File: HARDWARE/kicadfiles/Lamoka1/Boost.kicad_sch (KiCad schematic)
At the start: 35 parts, among them Q4 NMOS

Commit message: Improve on the values for the schematic of boost converter
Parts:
- C1: value C1206C474K5RACTU -> 0.47u
- C2: value CC0603KRX7R9BB223 -> 22n
- C25, C26: value UUX2A470MNL1GS -> 47u
- C27, C32: value UCD2A220MNL1GS -> 22u
- C28: value CL10B104KB8NNNC -> 100n
- C30: value KRM55WR72A226MH01L -> 22u
- C31: value UCD2A101MNJ1MS -> 10u
- Cbst7: value C1206C224M1REC7210 -> 220n
- Cbst8: value C1206C224M1REC7210 -> 0.22u
- Cvcc7: value CNC5L1X7R1H106K160AE -> 100n
- Cvcc8: value CNC5L1X7R1H106K160AE -> 10u
- R1: value RC0603FR-0756K2L -> 56.2k
- R2: value RN73R1JTTD1842F25 -> 18.4k
- R3: value RC0603FR-07392KL -> 392k
- R35, R37, R38: value RC0603FR-0736KL -> 36k
- R39, R40: value TLRP3A30CR005FTE -> 5m
- R4: value RC0603FR-0710KL -> 10k
- R5: value RN73R1JTTD4992F25 -> 49.9k
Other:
- moved on the sheet: C30, C31, C32, Q4, R38, R41

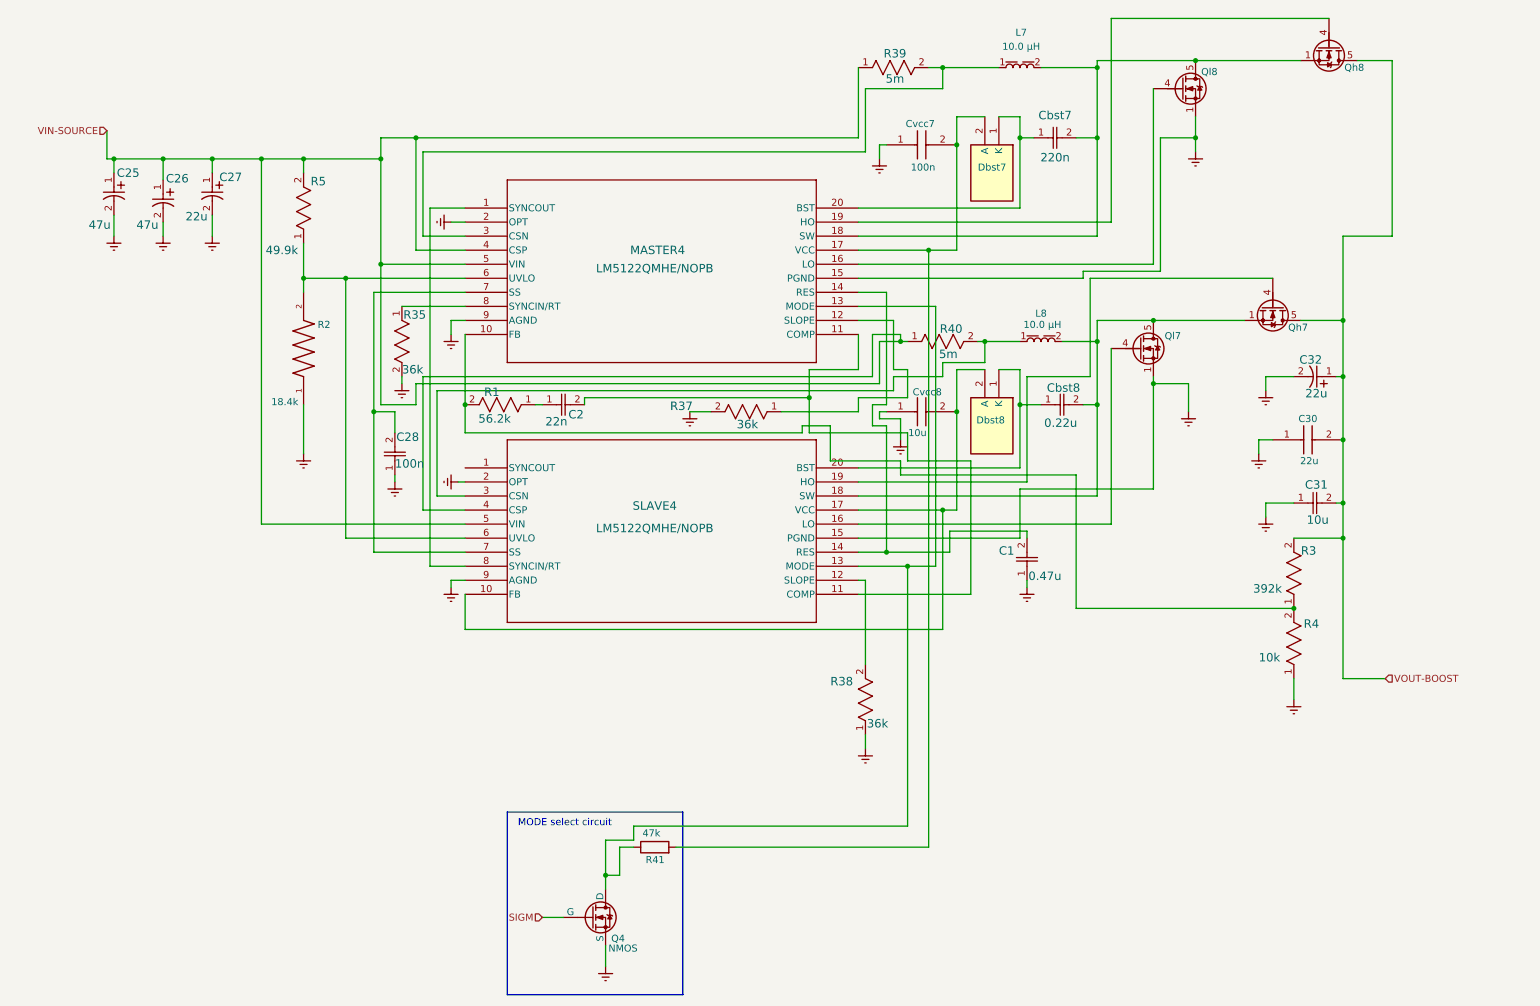
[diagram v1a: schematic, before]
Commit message: FIX values and add info
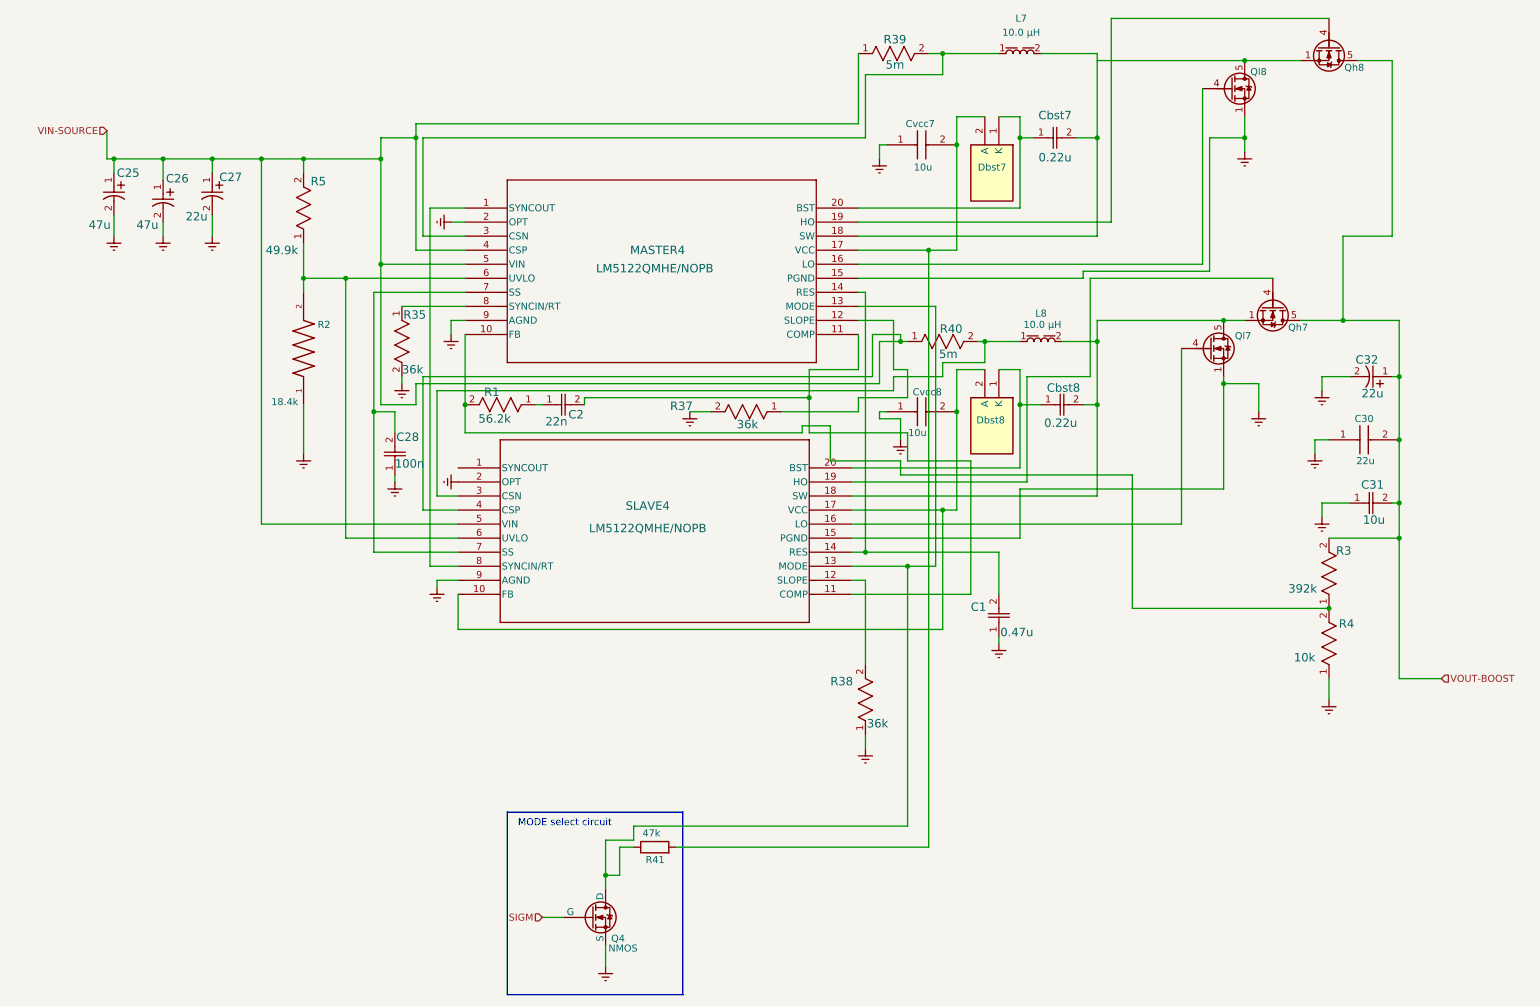
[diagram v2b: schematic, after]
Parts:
- Cbst7: value 220n -> 0.22u
- Cvcc7: value 100n -> 10u
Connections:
- net at Qh8.1 (S), Qh8.2 (S), Qh8.3 (S)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: no longer Cbst7.2, L7.2, MASTER4.18 (SW)
- new net: Cbst7.2, L7.2, MASTER4.18 (SW)
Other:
- company: (none) -> Flamingo-n-Cactus
- title: (none) -> Boost-section
- moved on the sheet: C1, C30, C31, C32, L7, Ql7, Ql8, R3, R39, R4, SLAVE4

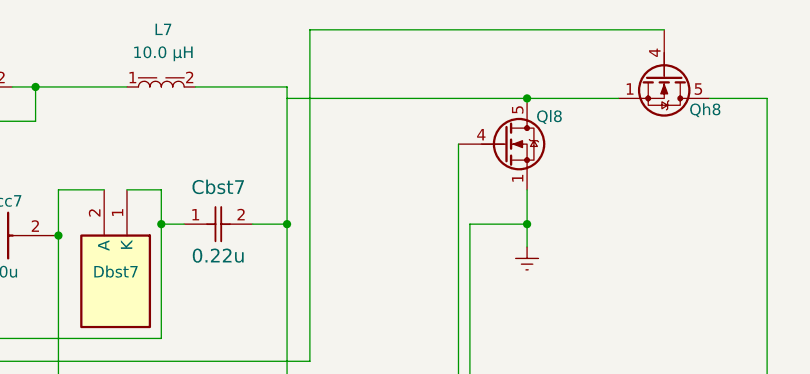
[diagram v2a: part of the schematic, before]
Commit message: URGENT had to fix a connection
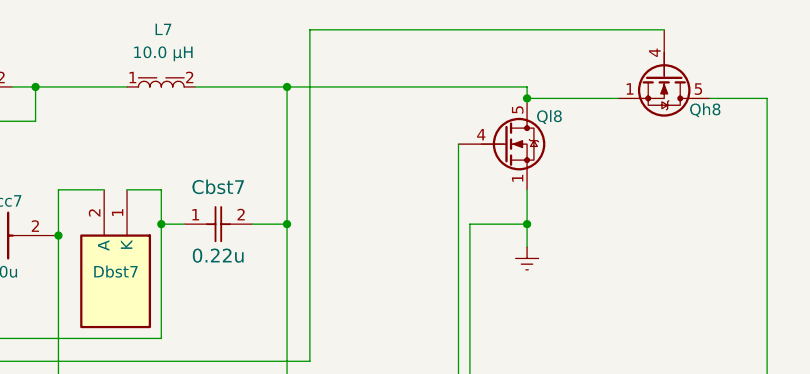
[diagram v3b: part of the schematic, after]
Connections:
- net at Qh8.1 (S), Qh8.2 (S), Qh8.3 (S)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: now also Cbst7.2, L7.2, MASTER4.18 (SW)
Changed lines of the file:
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@@
+	)
+	(junction
+		(at 205.74 22.86)
+		(diameter 0)
+		(color 0 0 0 0)
 	)
 	(junction
@@
 	(wire
 		(pts
-			(xy 205.74 24.13) (xy 232.41 24.13)
+			(xy 205.74 22.86) (xy 232.41 22.86)
 		)
 		(stroke
@@
 		)
 		(stroke
+			(width 0)
+			(type default)
+		)
+	)
+	(wire
+		(pts
+			(xy 232.41 22.86) (xy 232.41 24.13)
+		)
+		(stroke

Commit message: REAL actually fixing it for the net system
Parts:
- removed C28: 100n, Components:CAP_CL10_SAM, symbol 2026-06-24_20-27-18:CL10B104KB8NNNC
- removed C30: 22u, Components:CAPC6153X670N, symbol KRM55WR72A226MH01L:KRM55WR72A226MH01L
- removed C31: 10u, Components:CAP_UCD2A_NCH, symbol 2026-06-23_14-35-42:UCD2A101MNJ1MS
- removed C32: 22u, Components:PCAP_8x10-ELECT_NCH, symbol 2026-06-22_18-02-40:UCD2A220MNL1GS
- removed Q4: NMOS, symbol Simulation_SPICE:NMOS
- removed R35, R37: 36k, Components:RC0603N_YAG, symbol 2026-06-24_19-49-47:RC0603FR-0736KL
- added C29: 100n, Components:CAP_CL10_SAM, symbol 2026-06-24_20-27-18:CL10B104KB8NNNC
- added C33: 22u, Components:CAPC6153X670N, symbol KRM55WR72A226MH01L:KRM55WR72A226MH01L
- added C34: 10u, Components:CAP_UCD2A_NCH, symbol 2026-06-23_14-35-42:UCD2A101MNJ1MS
- added C35: 22u, Components:PCAP_8x10-ELECT_NCH, symbol 2026-06-22_18-02-40:UCD2A220MNL1GS
- added R36, R42: 36k, Components:RC0603N_YAG, symbol 2026-06-24_19-49-47:RC0603FR-0736KL
- added U1: AO3400A, Components:SOT-23-3L_AOS, symbol 2026-06-29_16-51-38:AO3400A
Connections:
- net Earth: now also C29.1, C33.1, C34.1, C35.2, R36.2, R42.2, U1.2 (S)
- net SIGM: now also U1.1 (G)
- net VOUT-BOOST: now also C33.2, C34.2, C35.1
- net BSTS: now reaches Cbst8.1, Dbst8.1 (K), SLAVE4.20 (BST)
- net SWS: now reaches Cbst8.2, L8.2, Qh7.1 (S), Qh7.2 (S), Qh7.3 (S), Ql7.5 (D), SLAVE4.18 (SW)
- net MODE: now reaches MASTER4.13 (MODE), R41.1, SLAVE4.13 (MODE)
- net MODE: now also U1.3 (D)
- net VCCM: now reaches Cvcc7.2, Dbst7.2 (A), MASTER4.17 (VCC), R41.2
- net BSTM: now reaches Cbst7.1, Dbst7.1 (K), MASTER4.20 (BST)
- net UVLO: now reaches MASTER4.6 (UVLO), R2.2, R5.1, SLAVE4.6 (UVLO)
- net SYNCIN/RTM: now reaches MASTER4.8 (SYNCIN/RT)
- net SYNCIN/RTM: now also R36.1
- net LOS: now reaches Ql7.4 (G), SLAVE4.16 (LO)
- net SS: now reaches MASTER4.7 (SS), SLAVE4.7 (SS)
- net SS: now also C29.2
- net FBS: now reaches Cvcc8.2, Dbst8.2 (A), SLAVE4.10 (FB), SLAVE4.17 (VCC)
- net FBM: now reaches MASTER4.10 (FB), R1.2, R3.1, R4.2
- net LOM: now reaches MASTER4.16 (LO), Ql8.4 (G)
- net SWM: now reaches Cbst7.2, L7.2, MASTER4.18 (SW), Qh8.1 (S), Qh8.2 (S), Qh8.3 (S), Ql8.5 (D)
- net HOM: now reaches MASTER4.19 (HO), Qh8.4 (G)
- net CSNS: now reaches L8.1, R40.2, SLAVE4.3 (CSN)
- net RES: now reaches C1.2, MASTER4.14 (RES), SLAVE4.14 (RES)
- net CSNM: now reaches L7.1, MASTER4.3 (CSN), R39.2
- net SYNCIN/RTS: now reaches MASTER4.1 (SYNCOUT), SLAVE4.8 (SYNCIN/RT)
- net COMP: now reaches C2.2, MASTER4.11 (COMP), SLAVE4.11 (COMP)
- net SLOPEM: now reaches MASTER4.12 (SLOPE)
- net SLOPEM: now also R42.1
- net HOS: now reaches Qh7.4 (G), SLAVE4.19 (HO)
- net SLOPES: now reaches R38.2, SLAVE4.12 (SLOPE)
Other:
- moved on the sheet: C1, C2, C25, C26, C27, Cbst7, Cbst8, Cvcc7, Cvcc8, Dbst7, Dbst8, L7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

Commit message: ADD more misc "housekeeping" work for boost converter
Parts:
- removed C34: 10u, Components:CAP_UCD2A_NCH, symbol 2026-06-23_14-35-42:UCD2A101MNJ1MS
- added C36: 10u, Components:CAP_UCD2A_NCH, symbol 2026-06-23_14-35-42:UCD2A101MNJ1MS
- added TP1, TP3, TP4, TP5: Tomachie_TP_N, TestPoint:TestPoint_Pad_D2.0mm, symbol Pads:Tomachie_TP_N
- added TP2: Tomachie_TP_S, TestPoint:TestPoint_Pad_D2.0mm, symbol Pads:Tomachie_TP_S
- added TP6, TP7, TP8: Tomachie_TP_W, TestPoint:TestPoint_Pad_D2.0mm, symbol Pads:Tomachie_TP_W
- L7, L8: Critical Parameter 10.0 µH -> 10u
- renumbered Cvcc7 to C3, Cbst7 to C4, Cvcc8 to C5, Cbst8 to C6, Dbst7 to D7, Dbst8 to D8, Ql8 to Q1, Qh8 to Q2, Ql7 to Q3, Qh7 to Q4, U1 to Q5, MASTER4 to U2, SLAVE4 to U3
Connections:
- net CSNM: now also TP1.1
- net CSNS: now also TP2.1
- net Earth: now also C36.2, TP3.1, TP4.1, TP5.1, TP6.1, TP7.1, TP8.1
- net VOUT-BOOST: now also C36.1
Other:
- note added: "SIGM = Connection to signal (MODE select)"
- note added: "VIN-SOURCE = 5-40V"
- note added: "VOUT-BOOST = 48v"
- moved on the sheet: C1, C2, C3, C33, C35, C4, C5, C6, D7, D8, L7, L8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

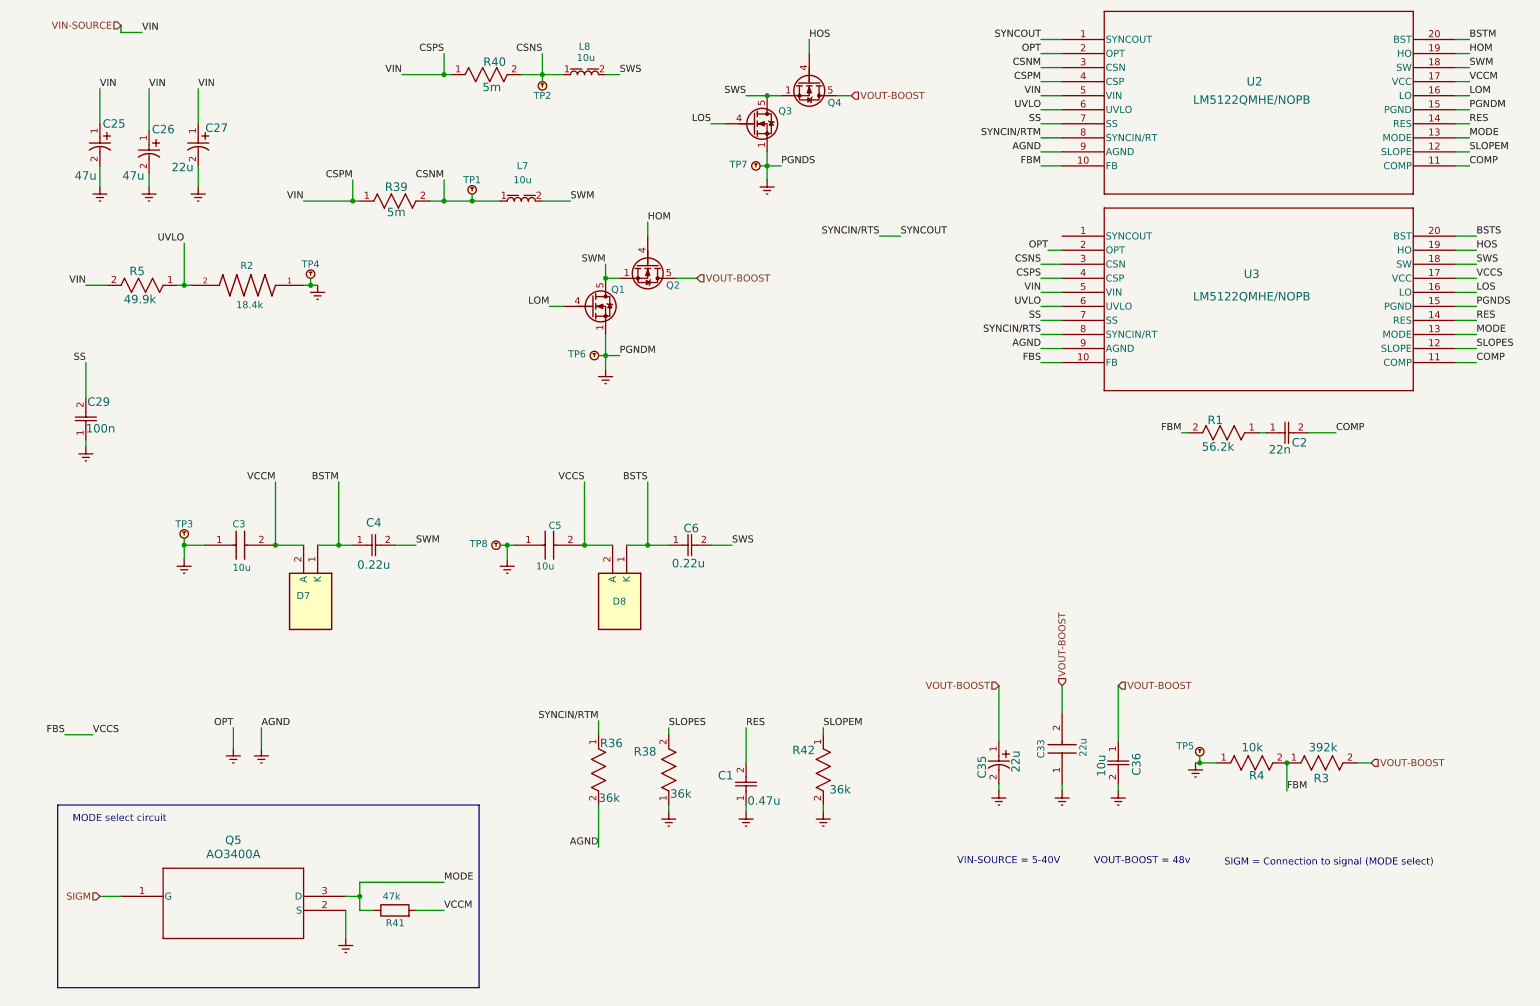
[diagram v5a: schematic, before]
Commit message: Make boost schem more neat, ADD top priority image
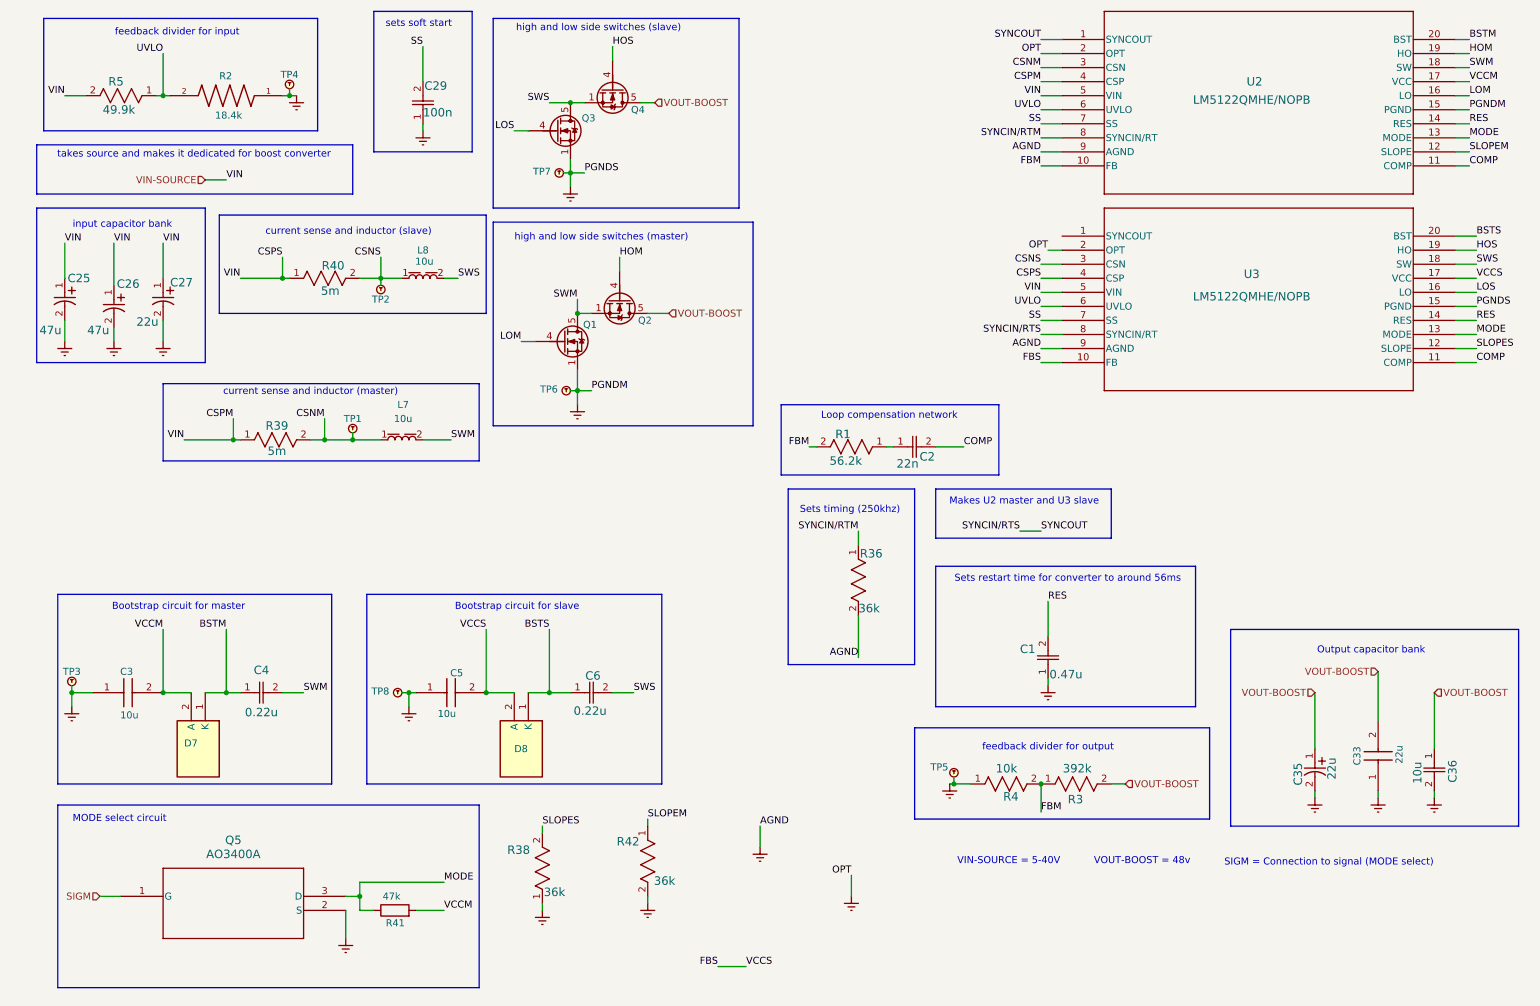
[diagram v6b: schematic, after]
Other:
- note added: "Bootstrap circuit for master"
- note added: "Bootstrap circuit for slave"
- note added: "Loop compensation network"
- note added: "Makes U2 master and U3 slave"
- note added: "Output capacitor bank"
- note added: "Sets restart time for converter to around 56ms"
- note added: "Sets timing (250khz)"
- note added: "current sense and inductor (master)"
- note added: "current sense and inductor (slave)"
- note added: "feedback divider for input"
- note added: "feedback divider for output"
- note added: "high and low side switches (master)"
- note added: "high and low side switches (slave)"
- note added: "input capacitor bank"
- note added: "sets soft start"
- note added: "takes source and makes it dedicated for boost converter"
- moved on the sheet: C1, C2, C25, C26, C27, C29, C3, C33, C35, C36, C4, C5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
